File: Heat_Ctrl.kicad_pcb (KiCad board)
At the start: 2 copper layers, 50 x 100 mm, 35 parts, among them K1 SRD-05VDC-SL-C, K2 SRD-05VDC-SL-C, P1 PWR, P2 DISPLAY, P3 IR_REC, P4 IIC_EXT, P5 Mains, P6 Touch, P7 TH1, P8 TH2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

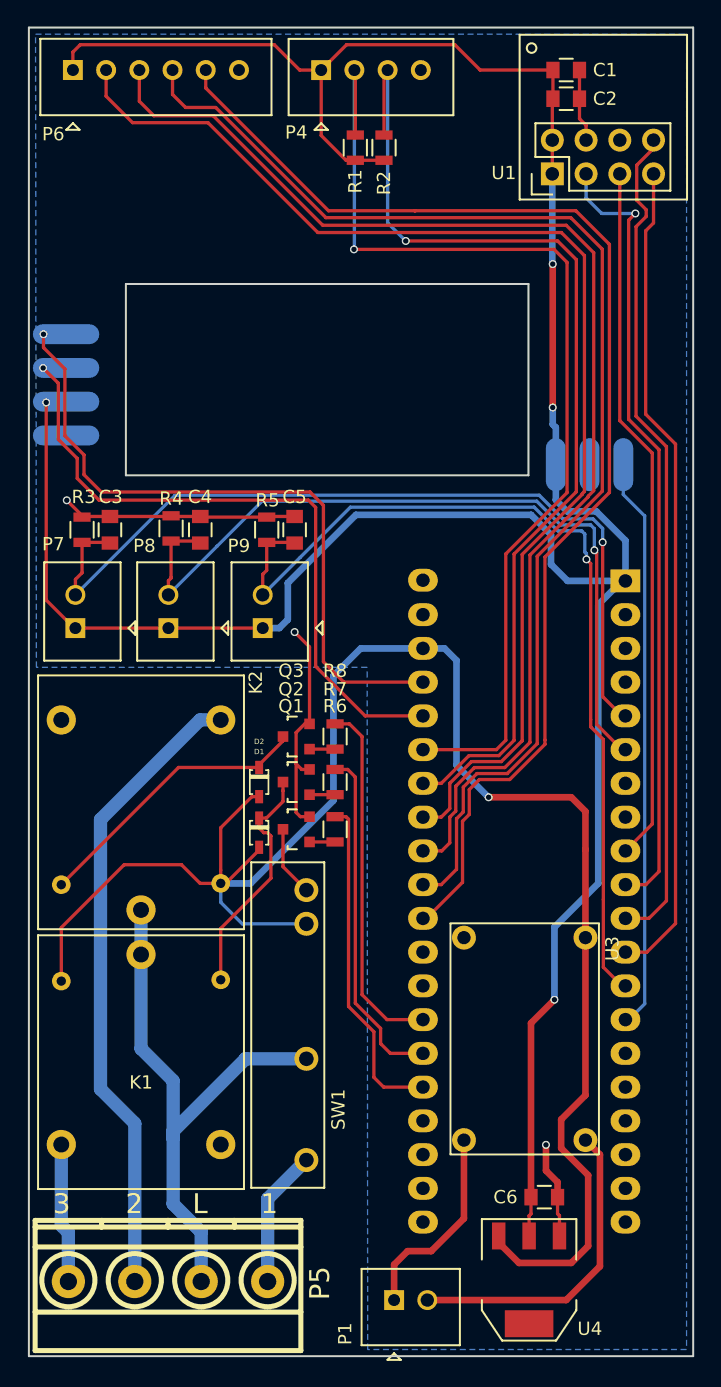
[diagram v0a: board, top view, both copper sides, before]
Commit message: IR Receiver Updates
Add pullup and buffer cap to IR receiver
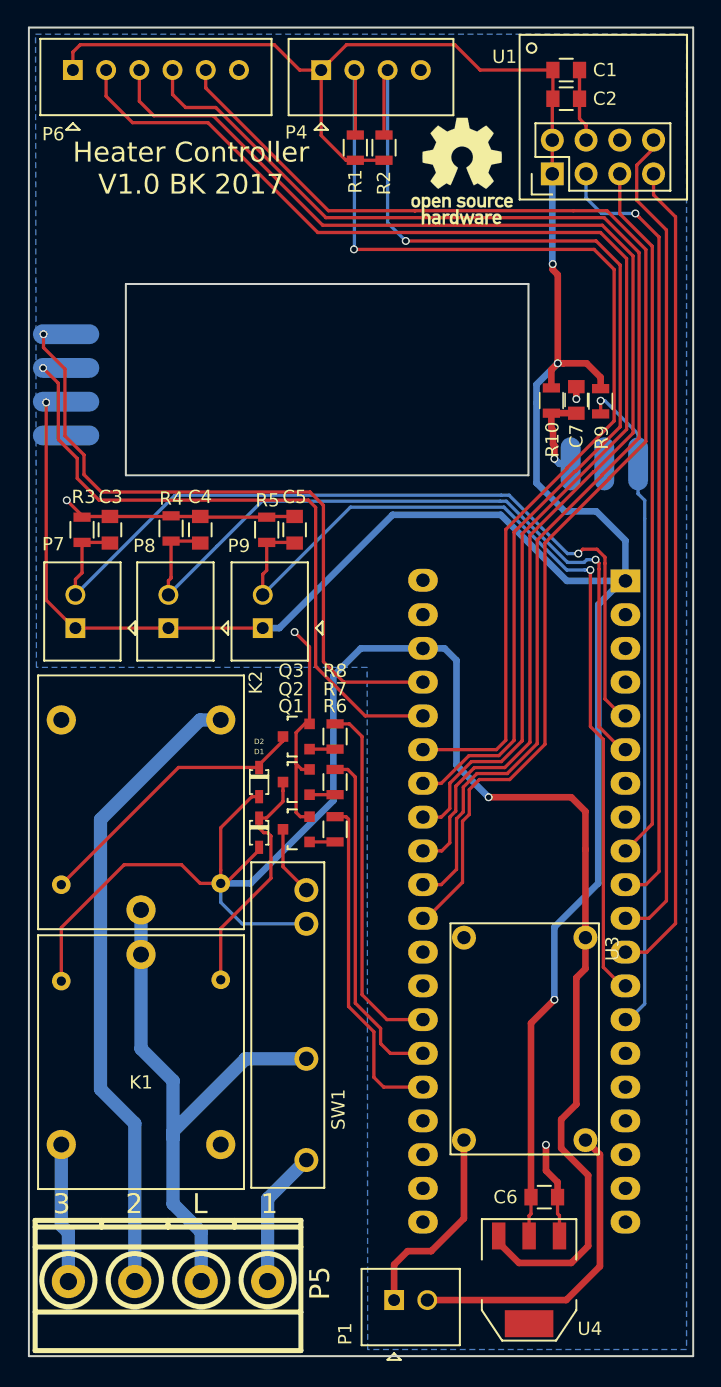
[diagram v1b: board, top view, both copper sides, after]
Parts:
- added C7: 1u, Capacitors_SMD:C_0805, F.Cu at (116.2, 69.0)
- added R10: 180, Resistors_SMD:R_0805, F.Cu at (114.3, 69.1)
- added R9: 10K, Resistors_SMD:R_0805, F.Cu at (118.0, 69.1)
- added REF***: KiCad-Logo2_6mm_SilkScreen, Symbols:KiCad-Logo2_6mm_SilkScreen, B.Cu at (93.5, 50.5)
- added REF***: OSHW-Logo_7.5x8mm_SilkScreen, Symbols:OSHW-Logo_7.5x8mm_SilkScreen, B.Cu at (81.5, 50.9)
- added REF***: OSHW-Logo_7.5x8mm_SilkScreen, Symbols:OSHW-Logo_7.5x8mm_SilkScreen, F.Cu at (107.6, 51.8)
- moved P3 1.11 mm to (118.3, 73.8)
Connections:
- P3 pad 3: +3V3 -> Net-(C7-Pad1)
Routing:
- net Net-(C7-Pad1): track 0.00 -> 6.79 mm, vias 0 -> 1
- net /IR_IN: track 43.2 -> 49.9 mm, vias 0 -> 1
- net +3V3: track 216.1 -> 221.9 mm
- net /SDA: track 79.3 -> 84.0 mm
- net /SCL: track 78.2 -> 82.6 mm
- net /T_4: track 92.4 -> 96.7 mm
- net /T_3: track 93.8 -> 97.9 mm
- net /T_2: track 94.6 -> 98.3 mm
- net /T_1: track 94.7 -> 98.3 mm
- net /TH3: track 69.4 -> 68.1 mm
- net /TH2: track 60.0 -> 58.9 mm
- net GND: track 47.7 -> 48.6 mm, vias 3 -> 4
- net /TH1: track 65.1 -> 64.2 mm
- net /MISO: track 63.0 -> 62.3 mm
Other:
- board text added: "HIGH VOLTAGE!"
- board text added: "Heater Controller V1.0 BK 2017"

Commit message: Display Change to TH
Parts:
- P2: footprint Heater_Ctrl:TM1637_Catalex -> Heater_Ctrl:TM1637_Catalex_TH
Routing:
- net /D_CLK: track 52.4 -> 48.3 mm, vias 1 -> 0
- net /D_DIO: track 53.3 -> 50.1 mm, vias 1 -> 0
- net GND: track 48.6 -> 51.7 mm, vias 4 -> 5
